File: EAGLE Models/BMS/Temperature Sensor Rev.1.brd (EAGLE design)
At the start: 160 x 100 mm, 25 parts

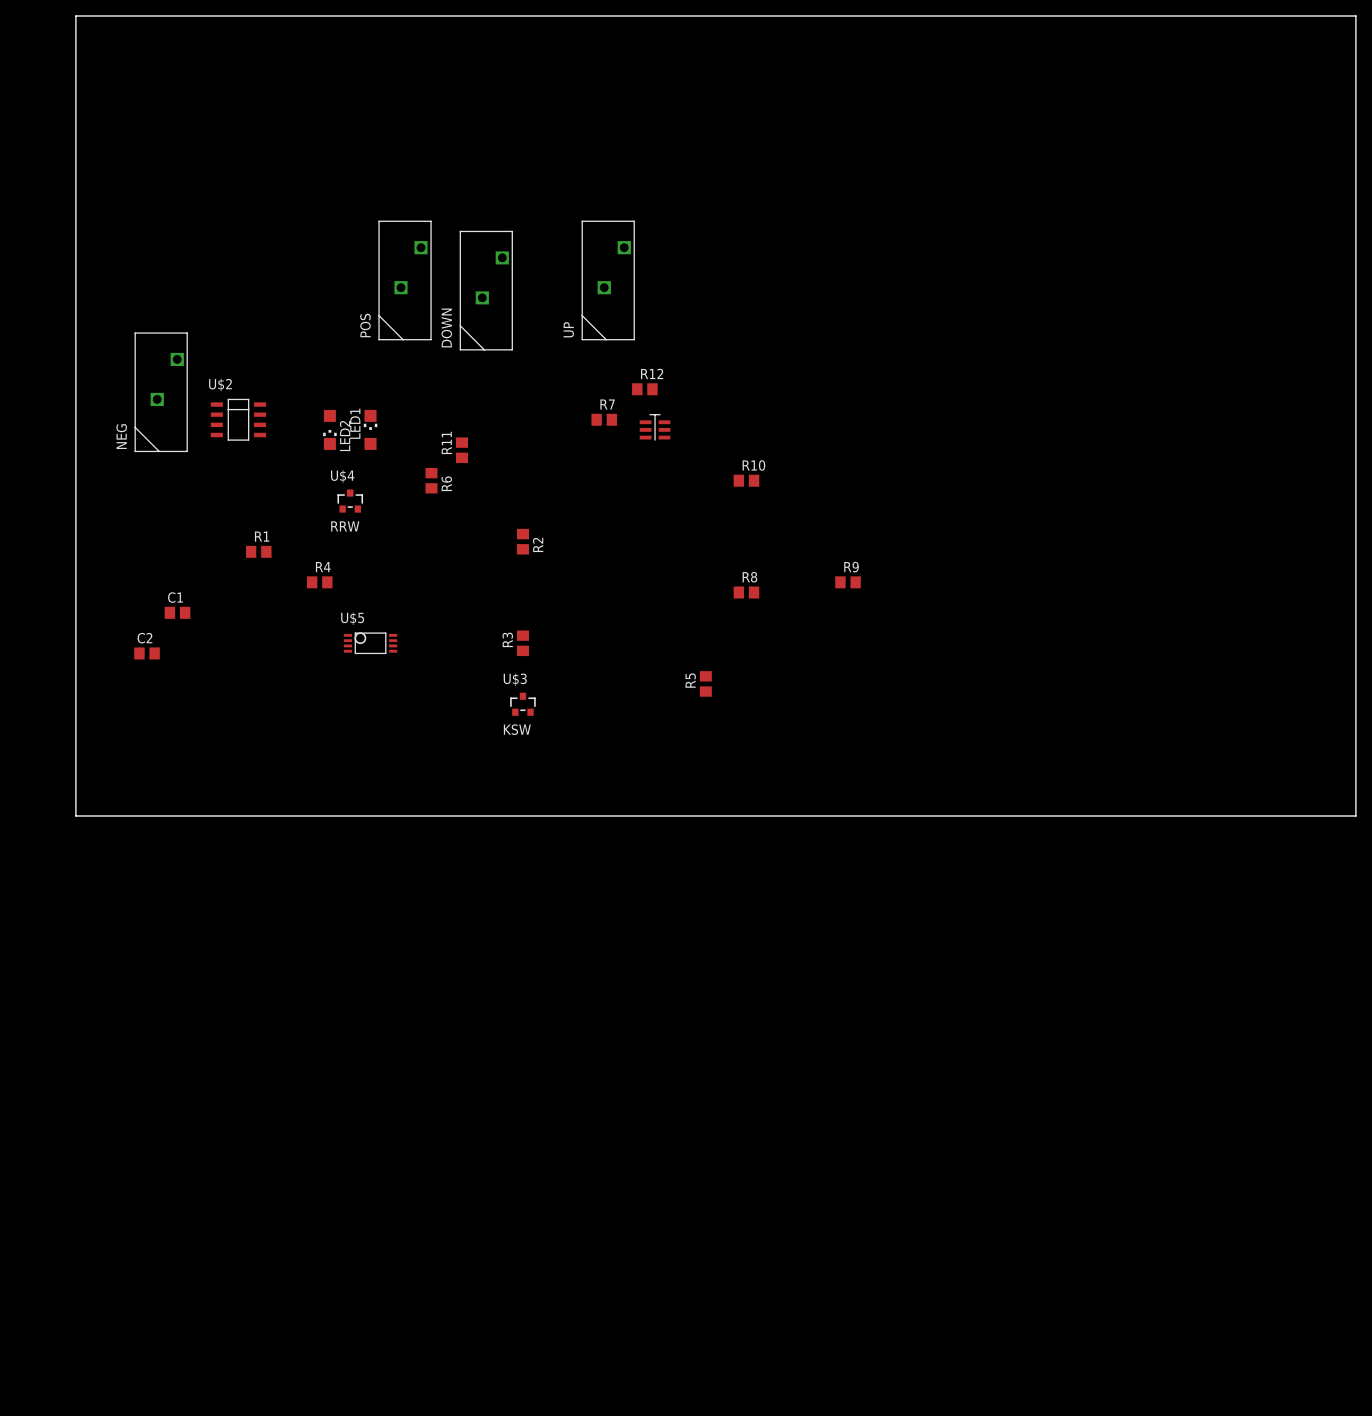
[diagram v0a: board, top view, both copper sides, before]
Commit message: Started schematic of temperature measurement circuit
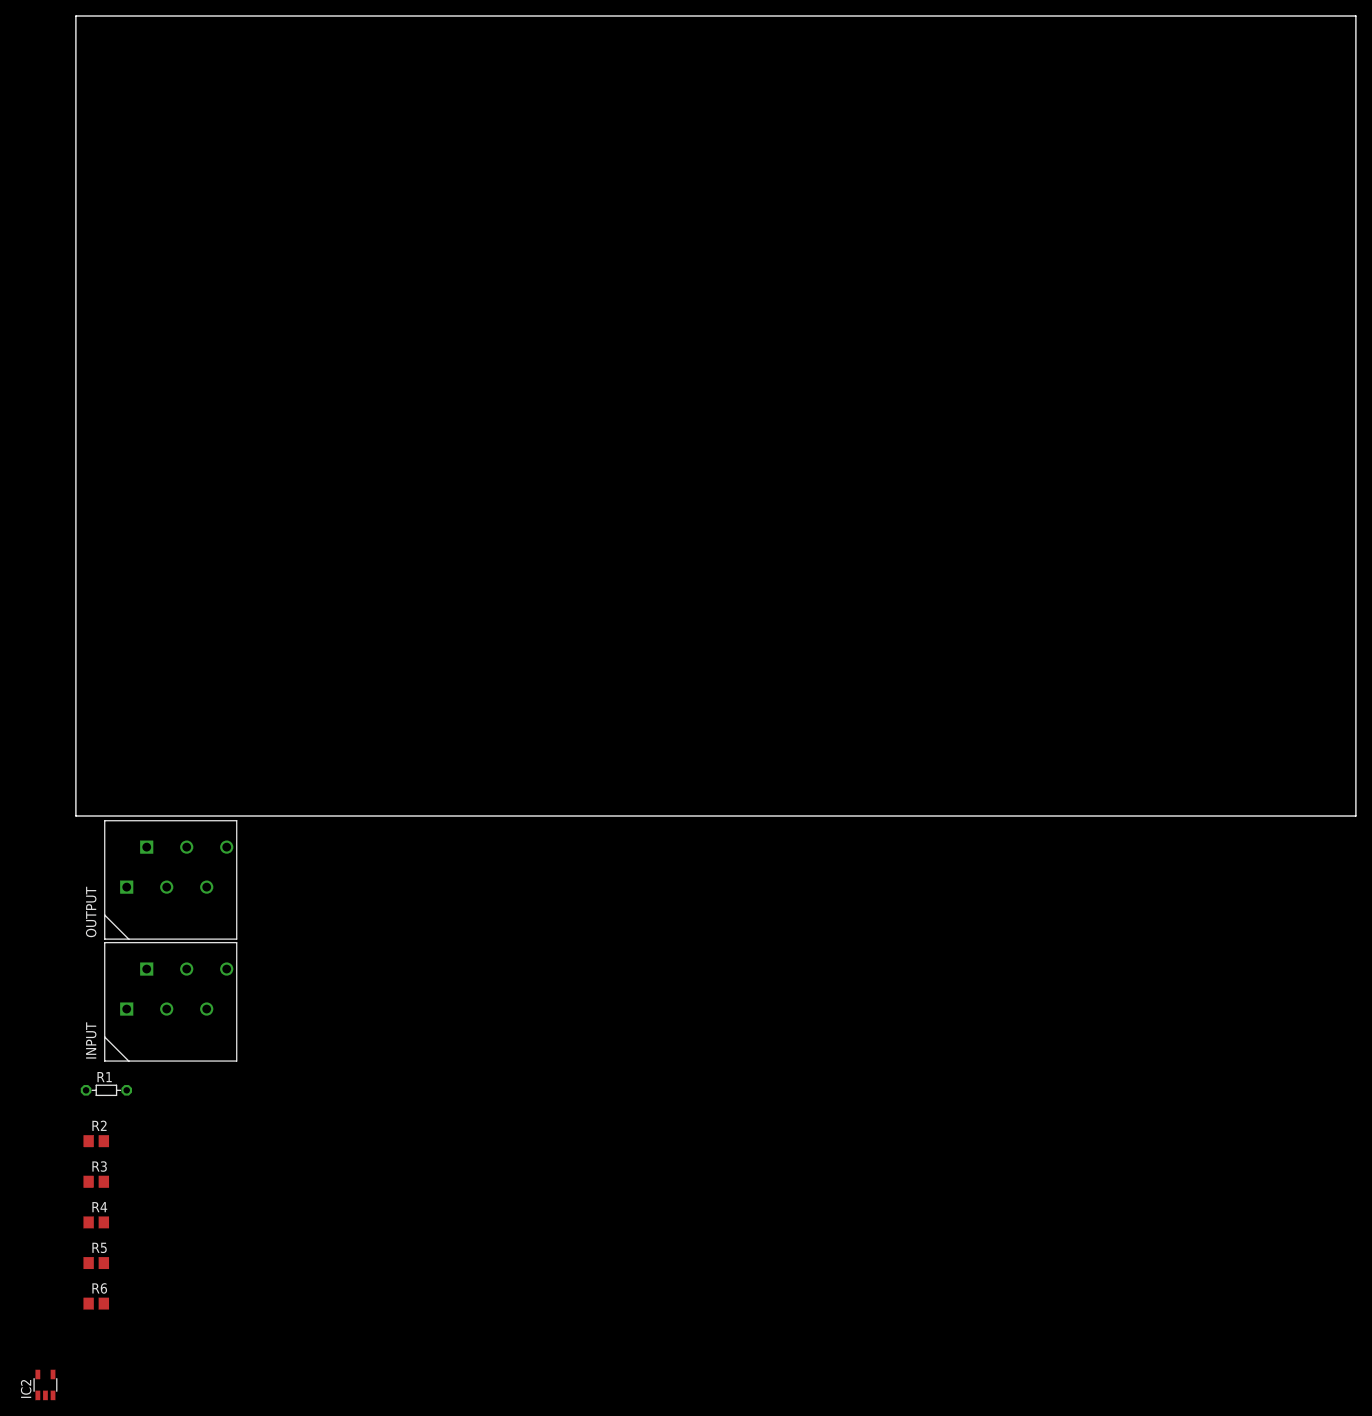
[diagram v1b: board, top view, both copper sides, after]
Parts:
- removed C1: (no value), resistor:C0805
- removed C2: 10-40Uf, resistor:C0805
- removed DOWN, NEG, POS, UP: CONN_1, formula electric:CONNECTOR_1
- removed LED1, LED2: (no value), led:CHIPLED_1206
- removed R10, R9: 1k, resistor:R0805
- removed R11, R8: 10k, resistor:R0805
- removed R12: 2.7, resistor:R0805
- removed R7: 10, resistor:R0805
- removed U$1: 23-T, BMS Lbr:SOT-23-6
- removed U$2: ATMEL285-1.2, BMS Lbr:8-SOIC
- removed U$3: KSW, BMS Lbr:SOT23-3
- removed U$4: RRW, BMS Lbr:SOT23-3
- removed U$5: T45V-10X-UP, BMS Lbr:TSOP-8
- added IC2: TL331, linear:DBV-R-PDSO-G5
- added INPUT, OUTPUT: CONN_3, formula electric:CONNECTOR_3
- R1: value 1K -> THERMISTOR-5; device resistor:R0805 -> varistor:R-5
- R2, R5, R6: value 10K -> (none)
- R3: value 1K -> (none)
- R4: value 10 -> (none)
- moved R6 111.1 mm to (2.54, -61.0), turned to 0 degrees
- moved R5 105.1 mm to (2.54, -55.9), turned to 0 degrees
- moved R2 92.0 mm to (2.54, -40.6), turned to 0 degrees
- moved R3 85.9 mm to (2.54, -45.7), turned to 0 degrees
- moved R4 84.7 mm to (2.54, -50.8)
- moved R1 70.0 mm to (3.81, -34.3)
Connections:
- removed net DOWN: DOWN.1, R1.1, R2.2
- removed net N$10: R4.1, R8.2, R9.2, U$5.P$3
- removed net N$11: LED1.A, R9.1
- removed net N$13: POS.1, R12.1, R7.1
- removed net N$14: R10.2, U$5.P$7
- removed net N$15: U$3.P$1, U$5.P$6
- removed net N$16: R11.1, U$5.P$1
- removed net N$3: R4.2, U$1.P$3
- removed net N$4: R3.1, U$3.P$2
- removed net N$6: R2.1, U$5.P$5
- removed net N$7: R5.2, U$5.P$2
- removed net N$8: C2.1, R5.1, R6.1, U$2.P$8
- removed net N$9: R12.2, U$1.P$1, U$1.P$2, U$1.P$5, U$1.P$6
- removed net UP: R3.2, UP.1
- new net INPUT: IC2.1, INPUT.3, INPUT.4
- new net OUTPUT: IC2.4, OUTPUT.3, OUTPUT.4
- net GND: now also IC2.2, INPUT.5, INPUT.6, OUTPUT.5, OUTPUT.6; no longer C1.2, C2.2, LED1.C, LED2.C, NEG.1, R8.1, U$1.P$4, U$2.P$4, U$3.P$3, U$4.P$3, U$5.P$4
- net N$1: now also IC2.3, R1.2, R3.2; no longer LED2.A, R10.1
- net VCC: now also IC2.5, INPUT.1, INPUT.2, OUTPUT.1, OUTPUT.2; no longer C1.1, R1.2, R11.2, R6.2, R7.2, U$4.P$1, U$4.P$2, U$5.P$8
